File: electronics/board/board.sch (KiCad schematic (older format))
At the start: 57 parts, among them J1 Screw_Terminal_01x02, J10 Conn_01x02, J11 Conn_01x02, J12 Conn_01x02, J13 Conn_01x02, J14 Conn_01x02, J15 Conn_01x02, J16 Conn_01x02, J17 Conn_01x02, J18 Conn_01x02, J19 Conn_01x02, J2 Screw_Terminal_01x02, J20 Conn_01x02, J21 Conn_01x02, J22 Conn_01x02, J25 Screw_Terminal_01x01, J3 AVR-ISP-6, J4 USB_B_Micro, J5 Screw_Terminal_01x02, J6 Screw_Terminal_01x02, J7 Conn_01x02, J8 Conn_01x02, J9 Conn_01x02, Q1 IRF7404, SW1 SW_Push_Open_Dual, U1 LMV358, U2 ATmega32U4-AU, U3 NCP1117-5.0_TO252, U4 ST485EBDR, U5 ULN2803A, U6 ULN2803A, Y1 Crystal 16MHz

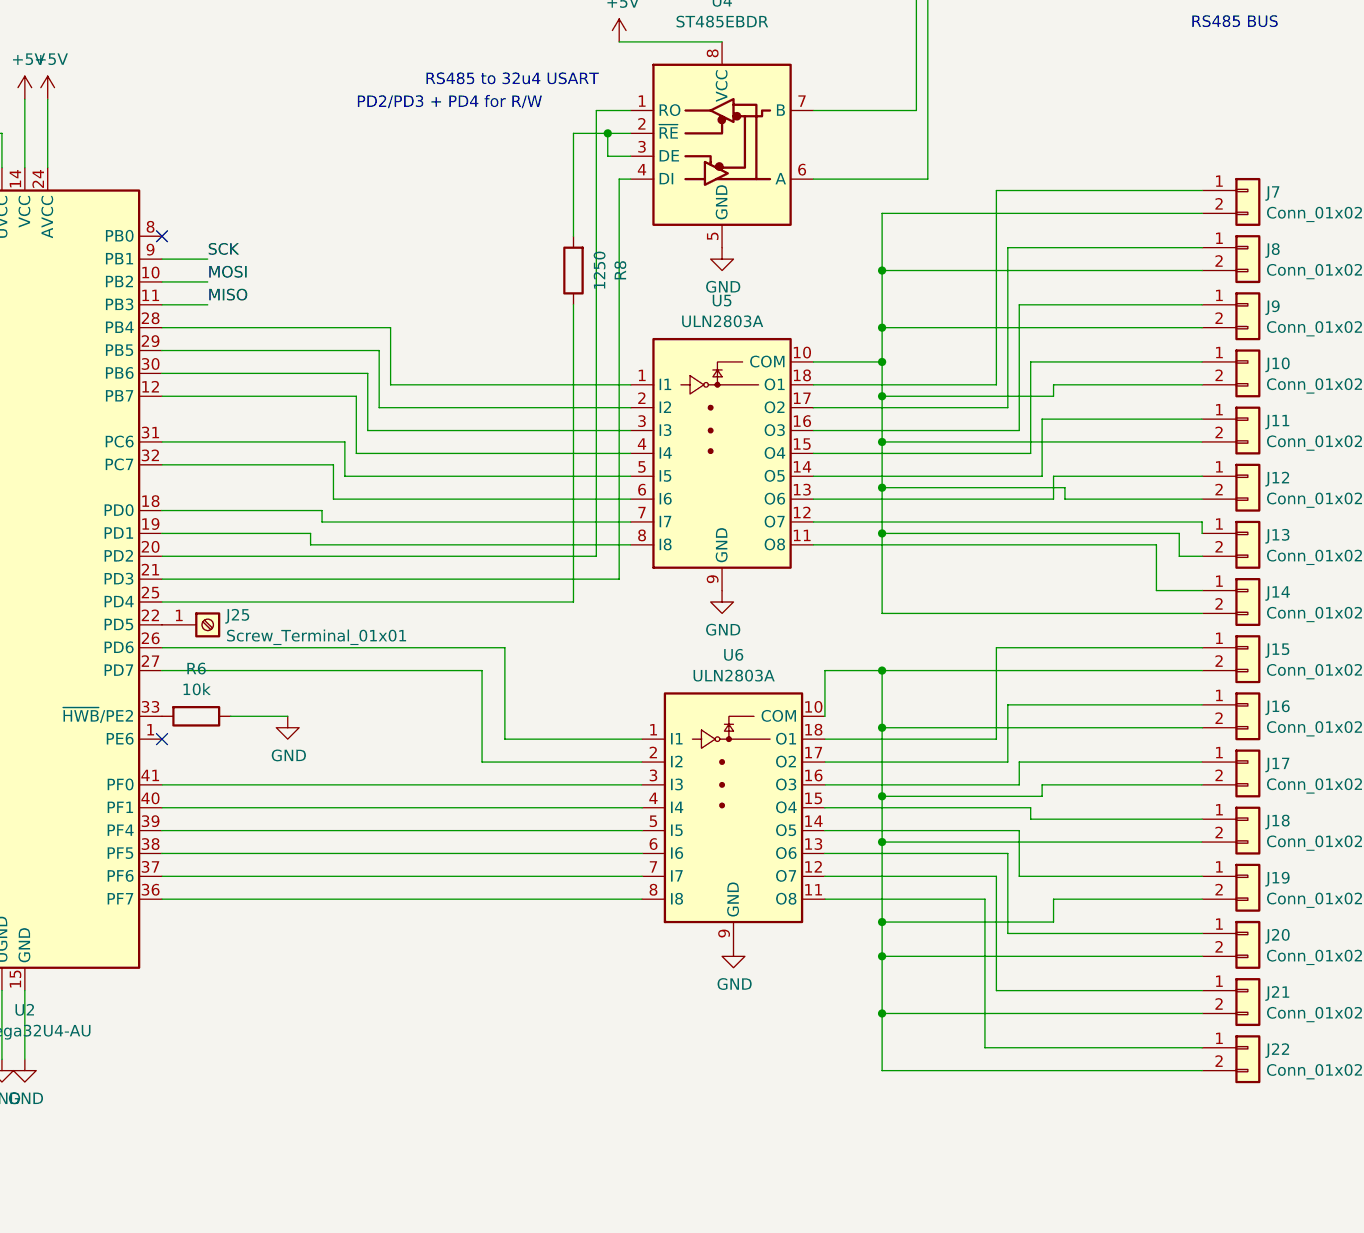
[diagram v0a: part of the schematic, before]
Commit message: Transistor fix + LEDs
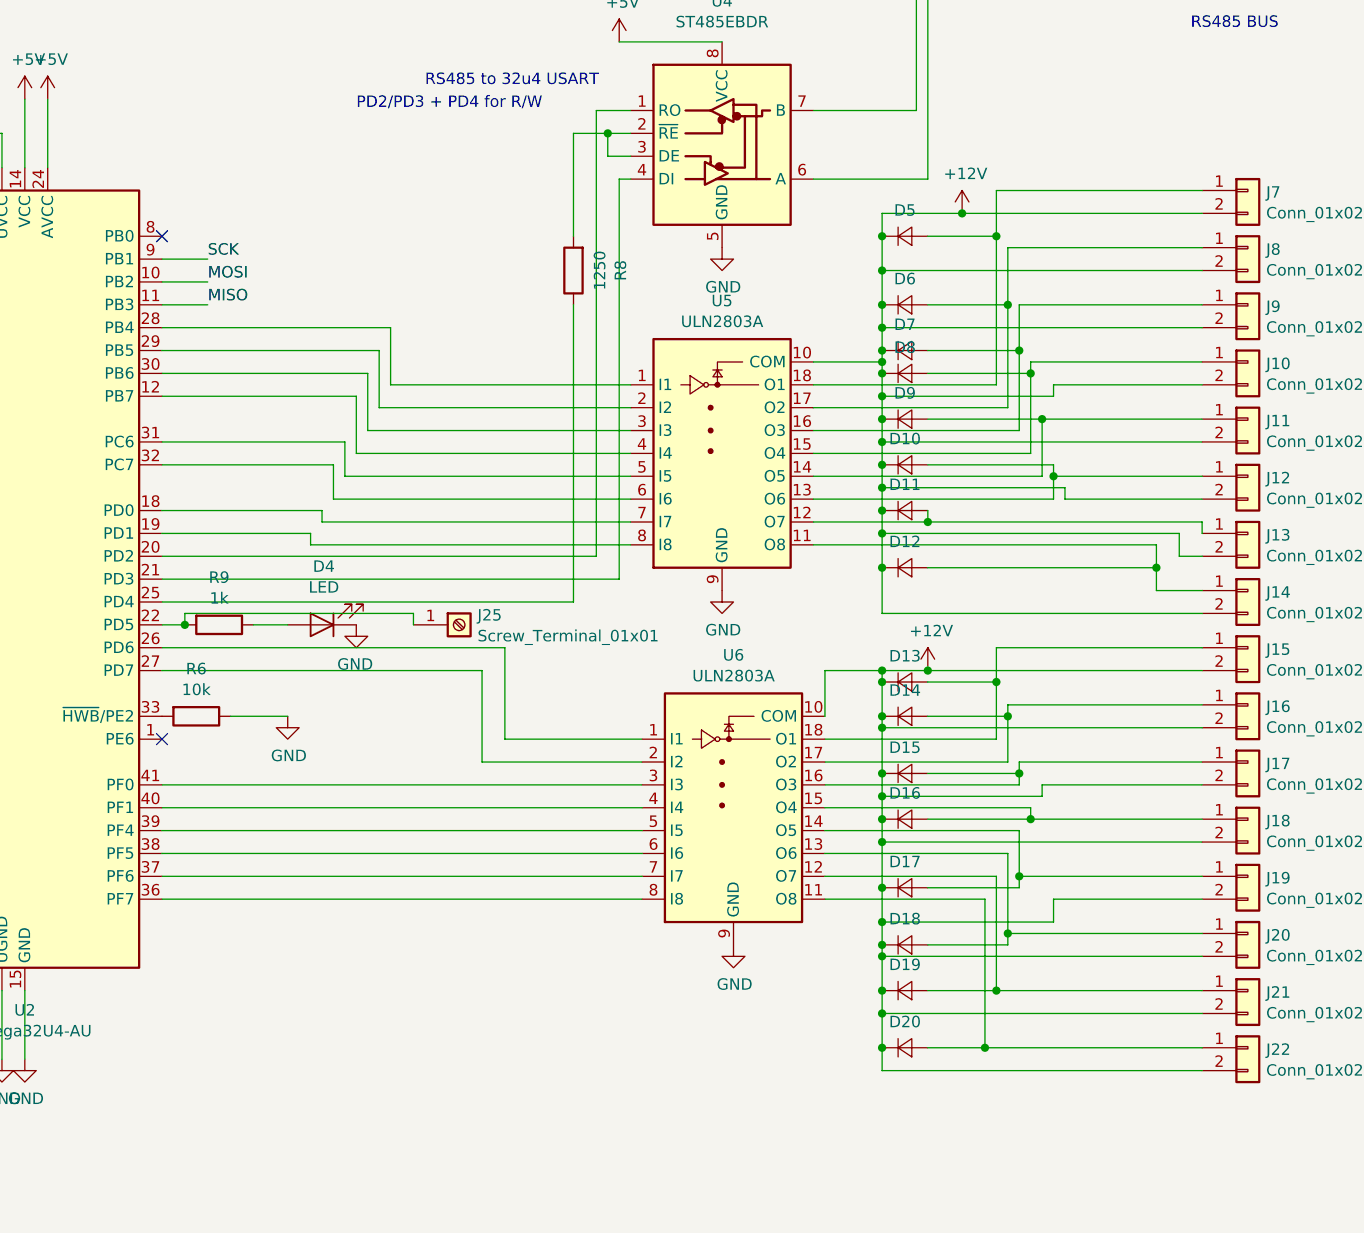
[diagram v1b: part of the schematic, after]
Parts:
- added D10, D11, D12, D13, D14, D15, D16, D17, D18, D19, D20, D5, D6, D7, D8, D9: D, symbol Device:D_Small
- added D4: LED, LED_SMD:LED_0805_2012Metric, symbol Device:LED
- added R9: 1k, Resistor_SMD:R_0603_1608Metric, symbol Device:R
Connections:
- net +12V: now also J10.2 (Pin_2), J11.2 (Pin_2), J12.2 (Pin_2), J13.2 (Pin_2), J14.2 (Pin_2), J15.2 (Pin_2), J16.2 (Pin_2), J17.2 (Pin_2), J18.2 (Pin_2), J19.2 (Pin_2), J20.2 (Pin_2), J21.2 (Pin_2), J22.2 (Pin_2), J7.2 (Pin_2), J8.2 (Pin_2), J9.2 (Pin_2), U5.10 (COM), U6.10 (COM), D10.1 (K), D11.1 (K), D12.1 (K), D13.1 (K), D14.1 (K), D15.1 (K), D16.1 (K), D17.1 (K), D18.1 (K), D19.1 (K), D20.1 (K), D5.1 (K), D6.1 (K), D7.1 (K), D8.1 (K), D9.1 (K)
- net GND: now also D4.1 (K)
- net at J14.1 (Pin_1), U5.11 (O8): now also D12.2 (A)
- net at J13.1 (Pin_1), U5.12 (O7): now also D11.2 (A)
- net at J12.1 (Pin_1), U5.13 (O6): now also D10.2 (A)
- net at J11.1 (Pin_1), U5.14 (O5): now also D9.2 (A)
- net at J10.1 (Pin_1), U5.15 (O4): now also D8.2 (A)
- net at J9.1 (Pin_1), U5.16 (O3): now also D7.2 (A)
- net at J8.1 (Pin_1), U5.17 (O2): now also D6.2 (A)
- net at J7.1 (Pin_1), U5.18 (O1): now also D5.2 (A)
- net at J22.1 (Pin_1), U6.11 (O8): now also D20.2 (A)
- net at J21.1 (Pin_1), U6.12 (O7): now also D19.2 (A)
- net at J20.1 (Pin_1), U6.13 (O6): now also D18.2 (A)
- net at J19.1 (Pin_1), U6.14 (O5): now also D17.2 (A)
- net at J18.1 (Pin_1), U6.15 (O4): now also D16.2 (A)
- net at J17.1 (Pin_1), U6.16 (O3): now also D15.2 (A)
- net at J16.1 (Pin_1), U6.17 (O2): now also D14.2 (A)
- net at J15.1 (Pin_1), U6.18 (O1): now also D13.2 (A)
- net at J25.1 (Pin_1), U2.22 (PD5): now also R9.2
- new net: D4.2 (A), R9.1
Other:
- moved on the sheet: J25

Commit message: Final routing and copper zones
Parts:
- D10, D11, D12, D13, D14, D15, D16, D17, D18, D19, D20, D5, D6, D7, D8, D9: footprint (none) -> Diode_SMD:D_0603_1608Metric_Pad1.05x0.95mm_HandSolder
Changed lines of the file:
@@
 F 0 "D5" H 9450 2813 50  0000 C CNN
 F 1 "D" V 9495 2768 50  0001 L CNN
-F 2 "" V 9450 2700 50  0001 C CNN
+F 2 "Diode_SMD:D_0603_1608Metric_Pad1.05x0.95mm_HandSolder" V 9450 2700 50  0001 C CNN
 F 3 "~" V 9450 2700 50  0001 C CNN
 	1    9450 2700
@@
 F 0 "D6" H 9450 3113 50  0000 C CNN
 F 1 "D" V 9495 3068 50  0001 L CNN
-F 2 "" V 9450 3000 50  0001 C CNN
+F 2 "Diode_SMD:D_0603_1608Metric_Pad1.05x0.95mm_HandSolder" V 9450 3000 50  0001 C CNN
 F 3 "~" V 9450 3000 50  0001 C CNN
 	1    9450 3000
@@
 F 0 "D7" H 9450 3313 50  0000 C CNN
 F 1 "D" V 9495 3268 50  0001 L CNN
-F 2 "" V 9450 3200 50  0001 C CNN
+F 2 "Diode_SMD:D_0603_1608Metric_Pad1.05x0.95mm_HandSolder" V 9450 3200 50  0001 C CNN
 F 3 "~" V 9450 3200 50  0001 C CNN
 	1    9450 3200
@@
 F 0 "D8" H 9450 3413 50  0000 C CNN
 F 1 "D" V 9495 3368 50  0001 L CNN
-F 2 "" V 9450 3300 50  0001 C CNN
+F 2 "Diode_SMD:D_0603_1608Metric_Pad1.05x0.95mm_HandSolder" V 9450 3300 50  0001 C CNN
 F 3 "~" V 9450 3300 50  0001 C CNN
 	1    9450 3300
@@
 F 0 "D9" H 9450 3613 50  0000 C CNN
 F 1 "D" V 9495 3568 50  0001 L CNN
-F 2 "" V 9450 3500 50  0001 C CNN
+F 2 "Diode_SMD:D_0603_1608Metric_Pad1.05x0.95mm_HandSolder" V 9450 3500 50  0001 C CNN
 F 3 "~" V 9450 3500 50  0001 C CNN
 	1    9450 3500
@@
 F 0 "D10" H 9450 3813 50  0000 C CNN
 F 1 "D" V 9495 3768 50  0001 L CNN
-F 2 "" V 9450 3700 50  0001 C CNN
+F 2 "Diode_SMD:D_0603_1608Metric_Pad1.05x0.95mm_HandSolder" V 9450 3700 50  0001 C CNN
 F 3 "~" V 9450 3700 50  0001 C CNN
 	1    9450 3700
@@
 F 0 "D11" H 9450 4013 50  0000 C CNN
 F 1 "D" V 9495 3968 50  0001 L CNN
-F 2 "" V 9450 3900 50  0001 C CNN
+F 2 "Diode_SMD:D_0603_1608Metric_Pad1.05x0.95mm_HandSolder" V 9450 3900 50  0001 C CNN
 F 3 "~" V 9450 3900 50  0001 C CNN
 	1    9450 3900
@@
 F 0 "D12" H 9450 4263 50  0000 C CNN
 F 1 "D" V 9495 4218 50  0001 L CNN
-F 2 "" V 9450 4150 50  0001 C CNN
+F 2 "Diode_SMD:D_0603_1608Metric_Pad1.05x0.95mm_HandSolder" V 9450 4150 50  0001 C CNN
 F 3 "~" V 9450 4150 50  0001 C CNN
 	1    9450 4150
@@
 F 0 "D14" H 9450 4913 50  0000 C CNN
 F 1 "D" V 9495 4868 50  0001 L CNN
-F 2 "" V 9450 4800 50  0001 C CNN
+F 2 "Diode_SMD:D_0603_1608Metric_Pad1.05x0.95mm_HandSolder" V 9450 4800 50  0001 C CNN
 F 3 "~" V 9450 4800 50  0001 C CNN
 	1    9450 4800
@@
 F 0 "D15" H 9450 5163 50  0000 C CNN
 F 1 "D" V 9495 5118 50  0001 L CNN
-F 2 "" V 9450 5050 50  0001 C CNN
+F 2 "Diode_SMD:D_0603_1608Metric_Pad1.05x0.95mm_HandSolder" V 9450 5050 50  0001 C CNN
 F 3 "~" V 9450 5050 50  0001 C CNN
 	1    9450 5050
@@
 F 0 "D16" H 9450 5363 50  0000 C CNN
 F 1 "D" V 9495 5318 50  0001 L CNN
-F 2 "" V 9450 5250 50  0001 C CNN
+F 2 "Diode_SMD:D_0603_1608Metric_Pad1.05x0.95mm_HandSolder" V 9450 5250 50  0001 C CNN
 F 3 "~" V 9450 5250 50  0001 C CNN
 	1    9450 5250
@@
 F 0 "D17" H 9450 5663 50  0000 C CNN
 F 1 "D" V 9495 5618 50  0001 L CNN
-F 2 "" V 9450 5550 50  0001 C CNN
+F 2 "Diode_SMD:D_0603_1608Metric_Pad1.05x0.95mm_HandSolder" V 9450 5550 50  0001 C CNN
 F 3 "~" V 9450 5550 50  0001 C CNN
 	1    9450 5550
@@
 F 0 "D18" H 9450 5913 50  0000 C CNN
 F 1 "D" V 9495 5868 50  0001 L CNN
-F 2 "" V 9450 5800 50  0001 C CNN
+F 2 "Diode_SMD:D_0603_1608Metric_Pad1.05x0.95mm_HandSolder" V 9450 5800 50  0001 C CNN
 F 3 "~" V 9450 5800 50  0001 C CNN
 	1    9450 5800
@@
 F 0 "D19" H 9450 6113 50  0000 C CNN
 F 1 "D" V 9495 6068 50  0001 L CNN
-F 2 "" V 9450 6000 50  0001 C CNN
+F 2 "Diode_SMD:D_0603_1608Metric_Pad1.05x0.95mm_HandSolder" V 9450 6000 50  0001 C CNN
 F 3 "~" V 9450 6000 50  0001 C CNN
 	1    9450 6000
@@
 F 0 "D20" H 9450 6363 50  0000 C CNN
 F 1 "D" V 9495 6318 50  0001 L CNN
-F 2 "" V 9450 6250 50  0001 C CNN
+F 2 "Diode_SMD:D_0603_1608Metric_Pad1.05x0.95mm_HandSolder" V 9450 6250 50  0001 C CNN
 F 3 "~" V 9450 6250 50  0001 C CNN
 	1    9450 6250
@@
 F 0 "D13" H 9450 4763 50  0000 C CNN
 F 1 "D" V 9495 4718 50  0001 L CNN
-F 2 "" V 9450 4650 50  0001 C CNN
+F 2 "Diode_SMD:D_0603_1608Metric_Pad1.05x0.95mm_HandSolder" V 9450 4650 50  0001 C CNN
 F 3 "~" V 9450 4650 50  0001 C CNN
 	1    9450 4650

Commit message: Diode protects only MCU
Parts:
- C1, C11, C2, C3, C4, C5, C6, C7, C8, C9: footprint Capacitor_SMD:C_0603_1608Metric -> Capacitor_SMD:C_0805_2012Metric_Pad1.15x1.40mm_HandSolder
- D1: footprint Diode_SMD:D_0603_1608Metric -> Diode_SMD:D_0805_2012Metric_Pad1.15x1.40mm_HandSolder
- D10, D11, D12, D13, D14, D15, D16, D17, D18, D19, D20, D5, D6, D7, D8, D9: footprint Diode_SMD:D_0603_1608Metric_Pad1.05x0.95mm_HandSolder -> Diode_SMD:D_0805_2012Metric_Pad1.15x1.40mm_HandSolder
- D2: footprint Diode_SMD:D_1210_3225Metric -> Diode_SMD:D_1206_3216Metric_Pad1.42x1.75mm_HandSolder
- R1, R2, R3, R4, R5, R6, R7, R8, R9, RV1, RV2: footprint Resistor_SMD:R_0603_1608Metric -> Resistor_SMD:R_0805_2012Metric_Pad1.15x1.40mm_HandSolder
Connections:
- net +12V: now also D2.1 (K), J1.1 (Pin_1), J5.1 (Pin_1); no longer D2.2 (A), U3.3 (VI)
- new net: D2.2 (A), U3.3 (VI)

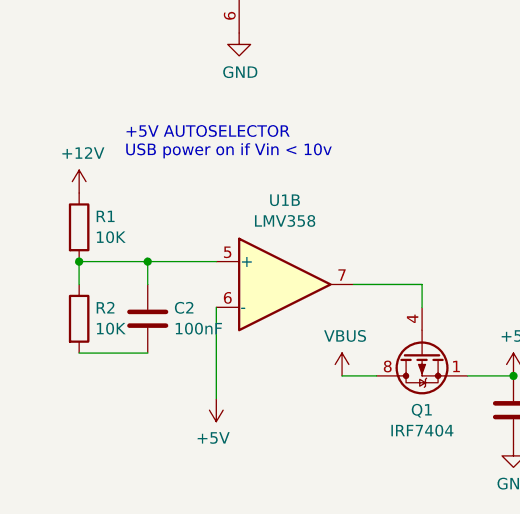
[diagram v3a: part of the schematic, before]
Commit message: Bugfixes R 10k and 12v track
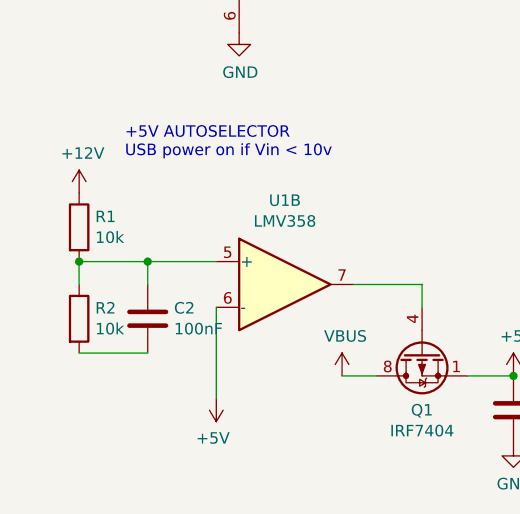
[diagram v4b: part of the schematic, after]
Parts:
- R1, R2: value 10K -> 10k
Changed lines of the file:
@@
 P 650 6250
 F 0 "R1" H 720 6296 50  0000 L CNN
-F 1 "10K" H 720 6205 50  0000 L CNN
+F 1 "10k" H 720 6205 50  0000 L CNN
 F 2 "Resistor_SMD:R_0805_2012Metric_Pad1.15x1.40mm_HandSolder" V 580 6250 50  0001 C CNN
 F 3 "~" H 650 6250 50  0001 C CNN
@@
 P 650 6650
 F 0 "R2" H 720 6696 50  0000 L CNN
-F 1 "10K" H 720 6605 50  0000 L CNN
+F 1 "10k" H 720 6605 50  0000 L CNN
 F 2 "Resistor_SMD:R_0805_2012Metric_Pad1.15x1.40mm_HandSolder" V 580 6650 50  0001 C CNN
 F 3 "~" H 650 6650 50  0001 C CNN

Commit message: Board v1.1 (not routed)
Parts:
- added C13, C8: 10uF, Capacitor_SMD:C_0805_2012Metric_Pad1.15x1.40mm_HandSolder, symbol Device:C
- C12: renamed from C10; value 10uF -> 100uF
- J10: renamed from J9; footprint Connector_JST:JST_ACH_BBM02B-ACHSS-GAN-ETF_1x02-1MP_P1.20mm_Vertical -> Custom JST XH:JST_XH_S2B-XH-A_1x02_P2.50mm_Horizontal
- J11: renamed from J10; footprint Connector_JST:JST_ACH_BBM02B-ACHSS-GAN-ETF_1x02-1MP_P1.20mm_Vertical -> Custom JST XH:JST_XH_S2B-XH-A_1x02_P2.50mm_Horizontal
- J12: renamed from J11; footprint Connector_JST:JST_ACH_BBM02B-ACHSS-GAN-ETF_1x02-1MP_P1.20mm_Vertical -> Custom JST XH:JST_XH_S2B-XH-A_1x02_P2.50mm_Horizontal
- J13: renamed from J12; footprint Connector_JST:JST_ACH_BBM02B-ACHSS-GAN-ETF_1x02-1MP_P1.20mm_Vertical -> Custom JST XH:JST_XH_S2B-XH-A_1x02_P2.50mm_Horizontal
- J14: renamed from J13; footprint Connector_JST:JST_ACH_BBM02B-ACHSS-GAN-ETF_1x02-1MP_P1.20mm_Vertical -> Custom JST XH:JST_XH_S2B-XH-A_1x02_P2.50mm_Horizontal
- J15: renamed from J14; footprint Connector_JST:JST_ACH_BBM02B-ACHSS-GAN-ETF_1x02-1MP_P1.20mm_Vertical -> Custom JST XH:JST_XH_S2B-XH-A_1x02_P2.50mm_Horizontal
- J16: renamed from J15; footprint Connector_JST:JST_ACH_BBM02B-ACHSS-GAN-ETF_1x02-1MP_P1.20mm_Vertical -> Custom JST XH:JST_XH_S2B-XH-A_1x02_P2.50mm_Horizontal
- J17: renamed from J16; footprint Connector_JST:JST_ACH_BBM02B-ACHSS-GAN-ETF_1x02-1MP_P1.20mm_Vertical -> Custom JST XH:JST_XH_S2B-XH-A_1x02_P2.50mm_Horizontal
- J18: renamed from J17; footprint Connector_JST:JST_ACH_BBM02B-ACHSS-GAN-ETF_1x02-1MP_P1.20mm_Vertical -> Custom JST XH:JST_XH_S2B-XH-A_1x02_P2.50mm_Horizontal
- J19: renamed from J18; footprint Connector_JST:JST_ACH_BBM02B-ACHSS-GAN-ETF_1x02-1MP_P1.20mm_Vertical -> Custom JST XH:JST_XH_S2B-XH-A_1x02_P2.50mm_Horizontal
- J20: renamed from J19; footprint Connector_JST:JST_ACH_BBM02B-ACHSS-GAN-ETF_1x02-1MP_P1.20mm_Vertical -> Custom JST XH:JST_XH_S2B-XH-A_1x02_P2.50mm_Horizontal
- J21: renamed from J20; footprint Connector_JST:JST_ACH_BBM02B-ACHSS-GAN-ETF_1x02-1MP_P1.20mm_Vertical -> Custom JST XH:JST_XH_S2B-XH-A_1x02_P2.50mm_Horizontal
- J22: renamed from J21; footprint Connector_JST:JST_ACH_BBM02B-ACHSS-GAN-ETF_1x02-1MP_P1.20mm_Vertical -> Custom JST XH:JST_XH_S2B-XH-A_1x02_P2.50mm_Horizontal
- J23: renamed from J22; footprint Connector_JST:JST_ACH_BBM02B-ACHSS-GAN-ETF_1x02-1MP_P1.20mm_Vertical -> Custom JST XH:JST_XH_S2B-XH-A_1x02_P2.50mm_Horizontal
- J5: renamed from J25; value Screw_Terminal_01x01 -> PD1
- J8: renamed from J7; footprint Connector_JST:JST_ACH_BBM02B-ACHSS-GAN-ETF_1x02-1MP_P1.20mm_Vertical -> Custom JST XH:JST_XH_S2B-XH-A_1x02_P2.50mm_Horizontal
- J9: renamed from J8; footprint Connector_JST:JST_ACH_BBM02B-ACHSS-GAN-ETF_1x02-1MP_P1.20mm_Vertical -> Custom JST XH:JST_XH_S2B-XH-A_1x02_P2.50mm_Horizontal
- renumbered C8 to C10, C9 to C11, C11 to C9, D3 to D2, D4 to D3, D2 to D4, F3 to F1, J5 to J6, J6 to J7, R7 to R6, R6 to R7, R9 to R8, R8 to R9
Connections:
- net +12V: now also C12.1, C13.1
- net GND: now also C13.2, C8.2
- net VBUS: now also C8.1; no longer C12.1
- net at U5.1 (I1): now also U2.32 (PC7); no longer U2.28 (PB4)
- net at U5.2 (I2): now also U2.31 (PC6); no longer U2.29 (PB5)
- net at U5.4 (I4): now also U2.29 (PB5); no longer U2.12 (PB7)
- net at U5.5 (I5): now also U2.28 (PB4); no longer U2.31 (PC6)
- net at U5.6 (I6): now also U2.27 (PD7); no longer U2.32 (PC7)
- net at U5.7 (I7): now also U2.26 (PD6); no longer U2.18 (PD0)
- net at U5.8 (I8): now also U2.22 (PD5); no longer U2.19 (PD1)
- net at U6.1 (I1): now also U2.18 (PD0); no longer U2.26 (PD6)
- net at U6.2 (I2): now also U2.12 (PB7); no longer U2.27 (PD7)
- net at J5.1 (Pin_1), R8.2: now also U2.19 (PD1); no longer U2.22 (PD5)
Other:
- moved on the sheet: C12, D3, J5, R8
